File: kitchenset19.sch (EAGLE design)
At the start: 76 parts, among them IC1 AVR-MEGA8-PPTH, J1 POWER_JACKPTH, J2 FTDI Header, Y1 16Mhz

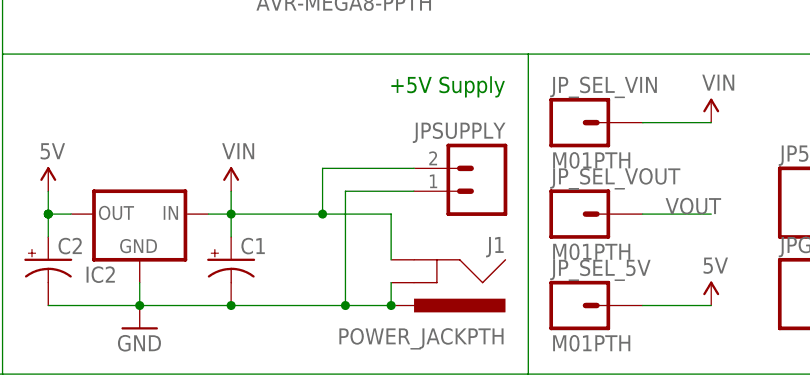
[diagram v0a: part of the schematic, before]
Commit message: fix incorrect pin assinments on DC barrel jack
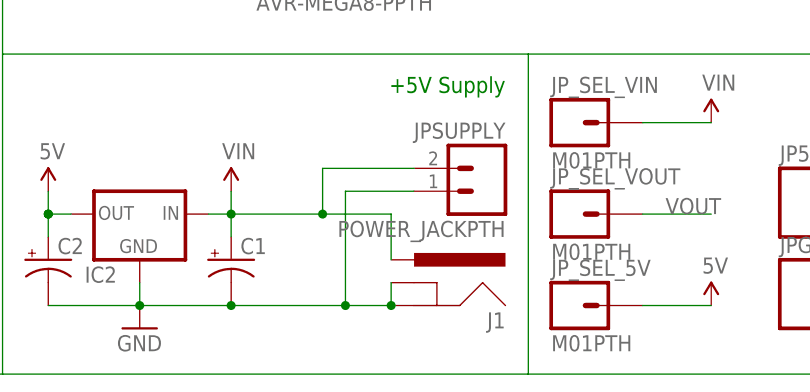
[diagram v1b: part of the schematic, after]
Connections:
- net GND: now also J1.GND; no longer J1.PWR
- net VIN: now also J1.PWR; no longer J1.GND
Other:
- moved on the sheet: J1
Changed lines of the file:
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@@
 <?xml version="1.0" encoding="utf-8"?>
 <!DOCTYPE eagle SYSTEM "eagle.dtd">
-<eagle version="6.2">
+<eagle version="6.4">
 <drawing>
 <settings>
@@
 <instance part="RESET_SW" gate="S" x="60.96" y="104.14" rot="MR0"/>
 <instance part="PWR_LED" gate="G$1" x="167.64" y="76.2" rot="MR270"/>
-<instance part="J1" gate="G$1" x="93.98" y="17.78" rot="R180"/>
+<instance part="J1" gate="G$1" x="93.98" y="7.62" rot="MR0"/>
 <instance part="GND1" gate="1" x="63.5" y="7.62"/>
 <instance part="P+1" gate="G$1" x="53.34" y="22.86"/>
@@
 <wire x1="63.5" y1="12.7" x2="63.5" y2="10.16" width="0.1524" layer="91"/>
 <junction x="63.5" y="10.16"/>
-<pinref part="J1" gate="G$1" pin="PWR"/>
 <wire x1="53.34" y1="10.16" x2="63.5" y2="10.16" width="0.1524" layer="91"/>
-<wire x1="91.44" y1="10.16" x2="86.36" y2="10.16" width="0.1524" layer="91"/>
 <wire x1="86.36" y1="10.16" x2="73.66" y2="10.16" width="0.1524" layer="91"/>
 <wire x1="63.5" y1="10.16" x2="73.66" y2="10.16" width="0.1524" layer="91"/>
@@
 <junction x="73.66" y="10.16"/>
 <pinref part="C2" gate="G$1" pin="-"/>
+<pinref part="JPSUPPLY" gate="G$1" pin="1"/>
+<wire x1="93.98" y1="22.86" x2="86.36" y2="22.86" width="0.1524" layer="91"/>
+<wire x1="86.36" y1="22.86" x2="86.36" y2="10.16" width="0.1524" layer="91"/>
+<pinref part="J1" gate="G$1" pin="GND"/>
+<wire x1="91.44" y1="10.16" x2="86.36" y2="10.16" width="0.1524" layer="91"/>
+<junction x="86.36" y="10.16"/>
 <pinref part="J1" gate="G$1" pin="GNDBREAK"/>
 <wire x1="91.44" y1="12.7" x2="91.44" y2="10.16" width="0.1524" layer="91"/>
 <junction x="91.44" y="10.16"/>
-<pinref part="JPSUPPLY" gate="G$1" pin="1"/>
-<wire x1="93.98" y1="22.86" x2="86.36" y2="22.86" width="0.1524" layer="91"/>
-<wire x1="86.36" y1="22.86" x2="86.36" y2="10.16" width="0.1524" layer="91"/>
-<junction x="86.36" y="10.16"/>
 </segment>
 <segment>
@@
 <wire x1="71.12" y1="20.32" x2="73.66" y2="20.32" width="0.1524" layer="91"/>
 <pinref part="C1" gate="G$1" pin="+"/>
-<pinref part="J1" gate="G$1" pin="GND"/>
-<wire x1="91.44" y1="20.32" x2="91.44" y2="15.24" width="0.1524" layer="91"/>
 <pinref part="JPSUPPLY" gate="G$1" pin="2"/>
 <wire x1="93.98" y1="25.4" x2="83.82" y2="25.4" width="0.1524" layer="91"/>
 <wire x1="83.82" y1="25.4" x2="83.82" y2="20.32" width="0.1524" layer="91"/>
 <junction x="83.82" y="20.32"/>
-</segment>
-<segment>
+<pinref part="J1" gate="G$1" pin="PWR"/>
+<wire x1="91.44" y1="20.32" x2="91.44" y2="15.24" width="0.1524" layer="91"/>
+</segment>
+<segment>
